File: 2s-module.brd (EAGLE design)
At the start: 19.4 x 48.2 mm, 36 parts, among them J1 CQ-USB-C16PSMT01, Q1 IRFR9020A, U1 MCP4725, U2 PC817XI, U3 LM393DR, U4 MICROCHIP_MIC5219-3_3YM5-TRMI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

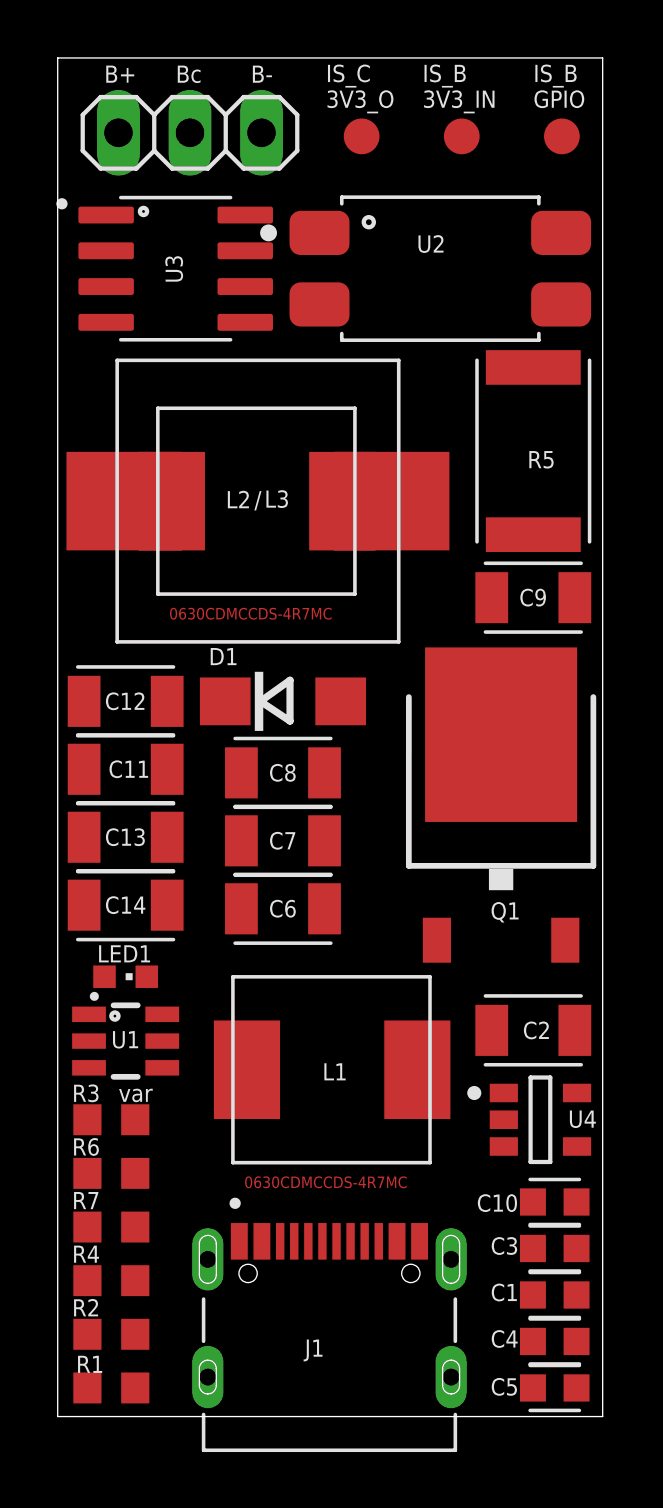
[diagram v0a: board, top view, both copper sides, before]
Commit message: route airwires
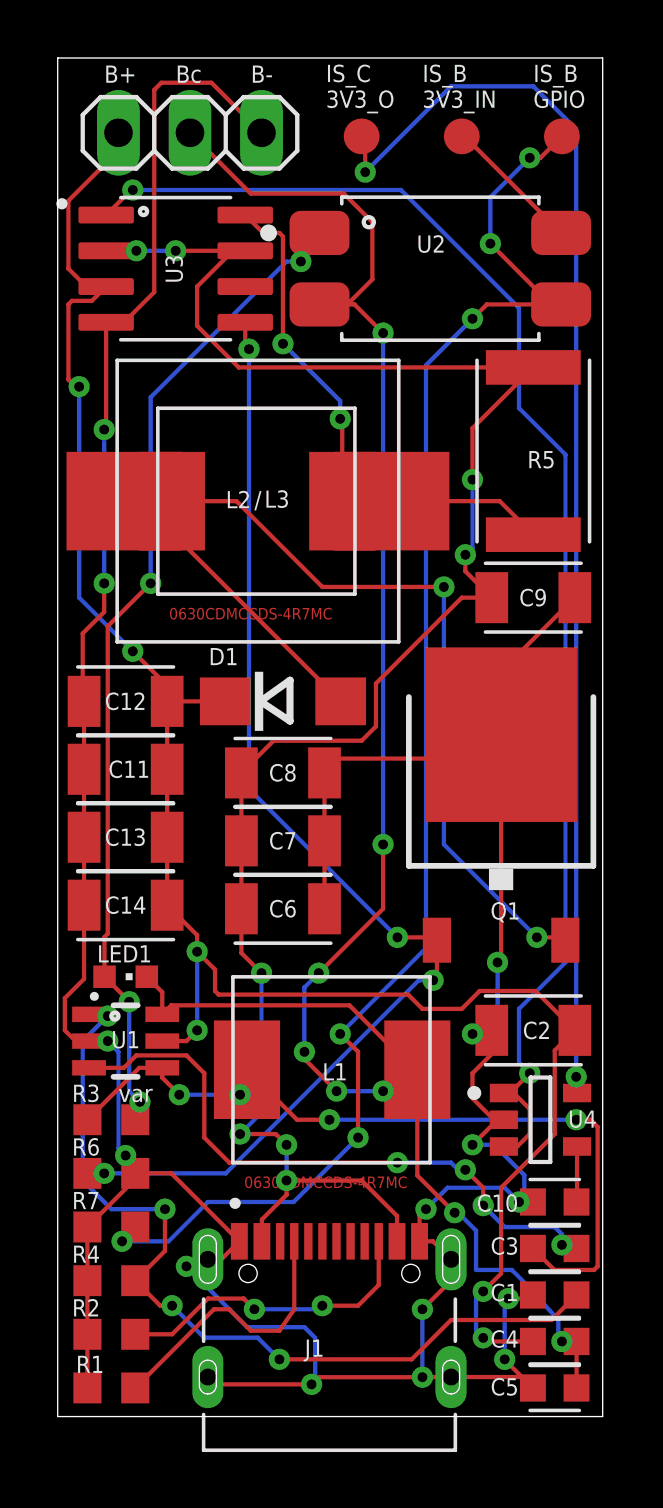
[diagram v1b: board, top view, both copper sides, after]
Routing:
- net GND: track 0.00 -> 135.3 mm, vias 0 -> 15
- net BATC: track 0.00 -> 72.9 mm, vias 0 -> 8
- net BATP: track 0.00 -> 69.8 mm, vias 0 -> 6
- net VBUS: track 0.00 -> 67.4 mm, vias 0 -> 8
- net IS_BALANCING_E_GPIO: track 0.00 -> 53.4 mm, vias 0 -> 6
- net STAT: track 0.00 -> 49.8 mm, vias 0 -> 2
- net IS_CHARGING_3V3_OUT: track 0.00 -> 45.0 mm, vias 0 -> 2
- net LDRV: track 0.00 -> 42.3 mm, vias 0 -> 4
- net D: track 0.00 -> 38.1 mm, vias 0 -> 2
- net N$1: track 0.00 -> 35.7 mm, vias 0 -> 4
- net ISET: track 0.00 -> 31.0 mm, vias 0 -> 4
- net SW: track 0.00 -> 28.7 mm, vias 0 -> 4
- net BIAS: track 0.00 -> 22.4 mm, vias 0 -> 4
- net CSN: track 0.00 -> 19.2 mm, vias 0 -> 2
- net CC2: track 0.00 -> 11.2 mm, vias 0 -> 2
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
